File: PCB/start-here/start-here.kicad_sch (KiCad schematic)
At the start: 23 parts, among them J1 RJ45_Hanrun_HR911105A_Horizon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, U1 STM32F439ZITx, U2 LAN8742A, U3 AP7361C-10E, Y1 Crystal_GND24

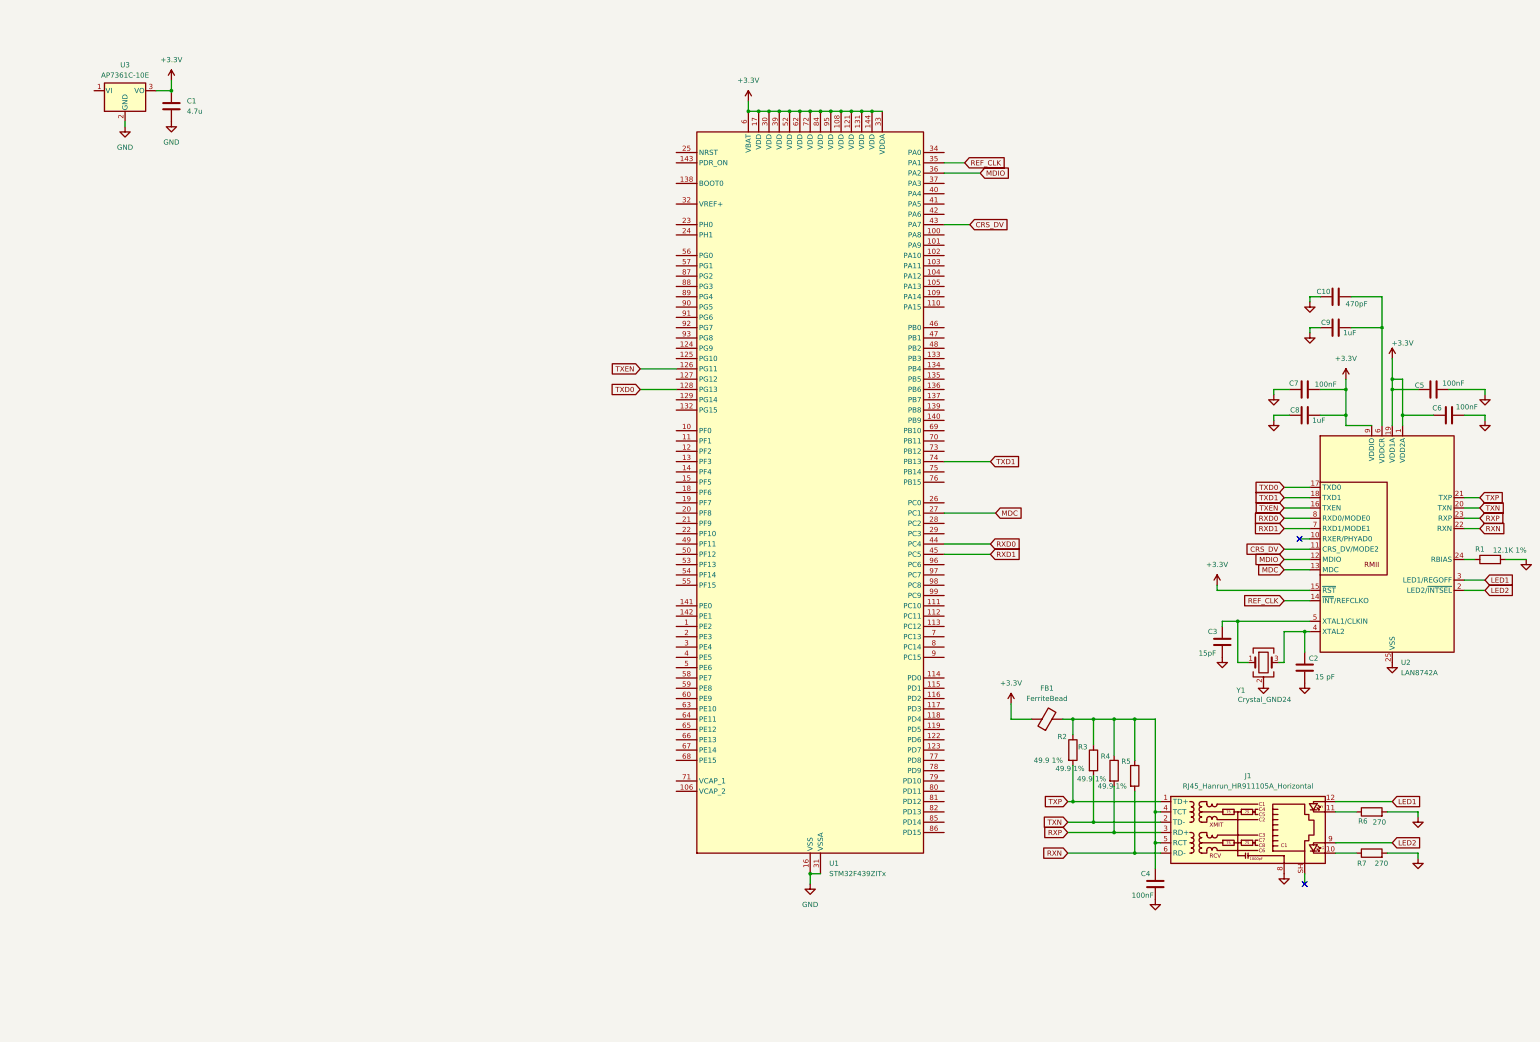
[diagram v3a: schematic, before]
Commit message: schematic done, but not verified
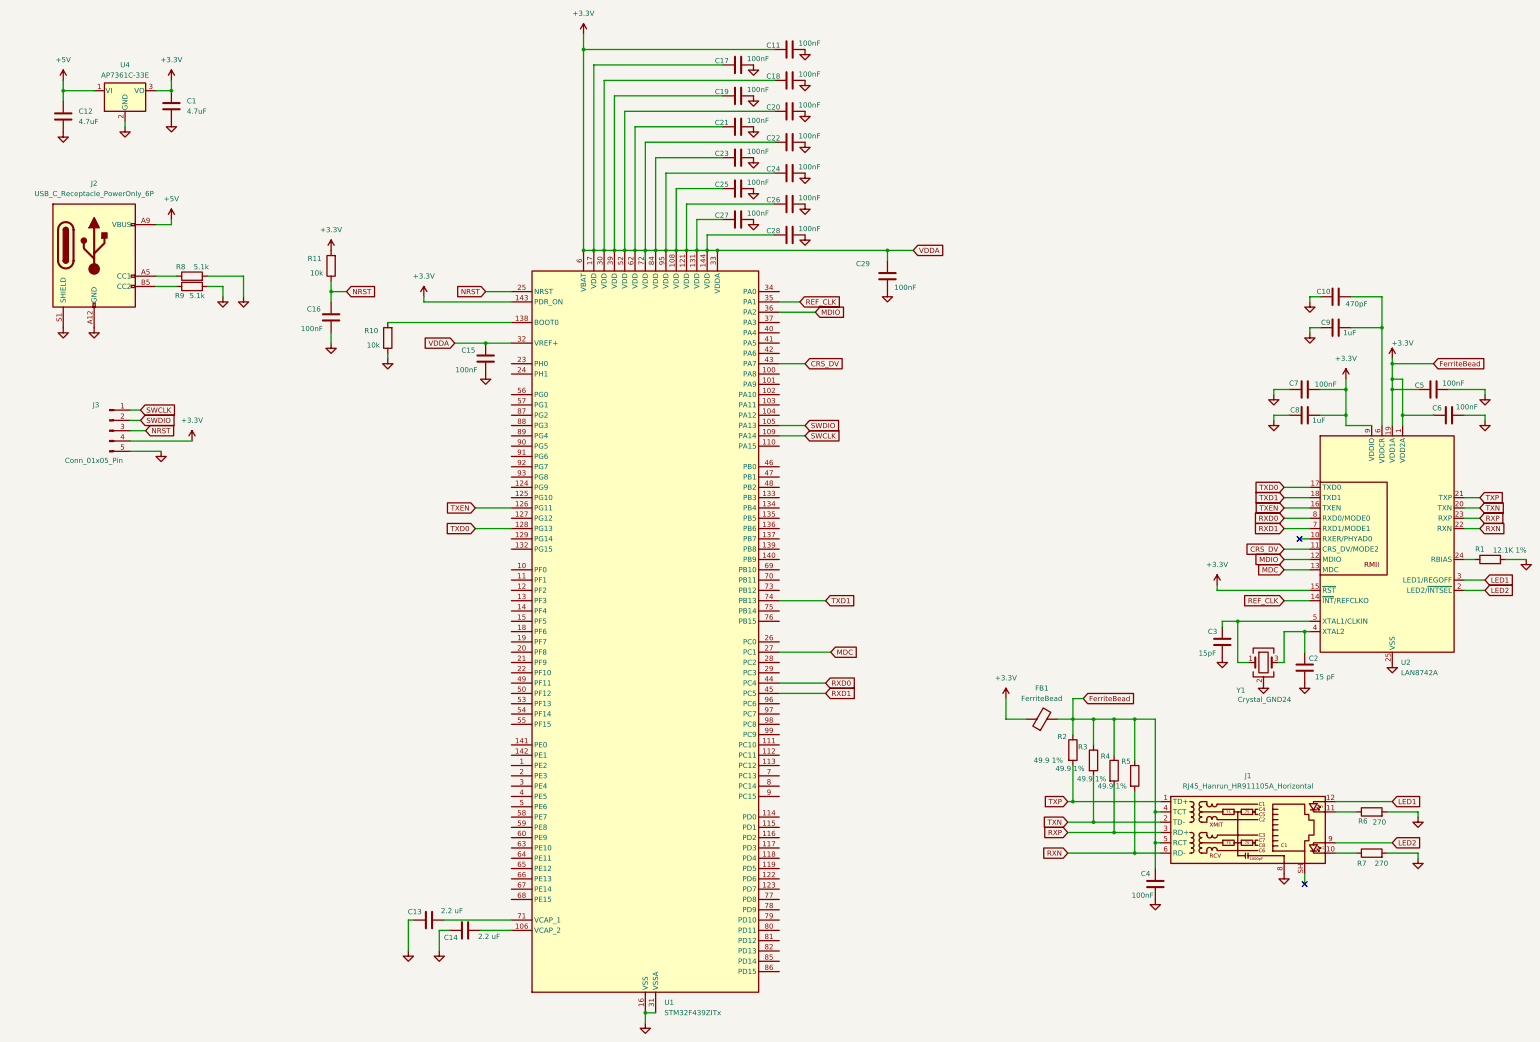
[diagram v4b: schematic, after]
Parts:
- removed U3: AP7361C-10E, Package_TO_SOT_SMD:SOT-223-3_TabPin2, symbol Regulator_Linear:AP7361C-10E
- added C11, C15, C16, C17, C18, C19, C20, C21, C22, C23, C24, C25, C26, C27, C28, C29: 100nF, symbol Device:C
- added C12: 4.7uF, Capacitor_SMD:C_1206_3216Metric, symbol Device:C
- added C13, C14: 2.2 uF, symbol Device:C
- added J2: USB_C_Receptacle_PowerOnly_6P, symbol Connector:USB_C_Receptacle_PowerOnly_6P
- added J3: Conn_01x05_Pin, symbol Connector:Conn_01x05_Pin
- added R10, R11: 10k, symbol Device:R
- added R8, R9: 5.1k, symbol Device:R
- added U4: AP7361C-33E, Package_TO_SOT_SMD:SOT-223-3_TabPin2, symbol Regulator_Linear:AP7361C-33E
- C1: value 4.7u -> 4.7uF
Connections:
- net +3.3V: now also C4.1, FB1.2, J1.4 (TCT), J1.5 (RCT), R2.1, R3.1, R4.1, R5.1, U1.143 (PDR_ON), U1.32 (VREF+), C11.1, C15.2, C17.1, C18.1, C19.1, C20.1, C21.1, C22.1, C23.1, C24.1, C25.1, C26.1, C27.1, C28.1, C29.2, J3.4 (Pin_4), R11.2, U4.3 (VO)
- net GND: now also C11.2, C12.2, C13.1, C14.1, C15.1, C16.1, C17.2, C18.2, C19.2, C20.2, C21.2, C22.2, C23.2, C24.2, C25.2, C26.2, C27.2, C28.2, C29.1, J2.A12 (GND), J2.B12 (GND), J2.S1 (SHIELD), J3.5 (Pin_5), R10.1, R8.2, R9.2, U4.2 (GND)
- net SWDIO: now reaches U1.105 (PA13)
- net SWDIO: now also J3.2 (Pin_2)
- net at U1.106 (VCAP_2): now also C14.2
- net SWCLK: now reaches U1.109 (PA14)
- net SWCLK: now also J3.1 (Pin_1)
- net at U1.138 (BOOT0): now also R10.2
- net NRST: now reaches U1.25 (NRST)
- net NRST: now also C16.2, J3.3 (Pin_3), R11.1
- net at U1.71 (VCAP_1): now also C13.2
- new net: J2.B5 (CC2), R9.1
- new net: J2.A5 (CC1), R8.1
- new net +5V: C12.1, J2.A9 (VBUS), J2.B9 (VBUS), U4.1 (VI)
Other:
- moved on the sheet: FB1, U1

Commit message: schematic done, no footprints
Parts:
- removed J3: Conn_01x05_Pin, symbol Connector:Conn_01x05_Pin
- added C3, C4: 100nF, symbol Device:C
- added J2: Conn_ARM_SWD_TagConnect_TC2030, Connector:Tag-Connect_TC2030-IDC-FP_2x03_P1.27mm_Vertical, symbol Connector:Conn_ARM_SWD_TagConnect_TC2030
- J1: renamed from J2; footprint (none) -> Connector_USB:USB_C_Receptacle_GCT_USB4125-xx-x-0190_6P_TopMnt_Horizontal
- renumbered C12 to C1, C19 to C10, C21 to C11, C23 to C12, C25 to C13, C27 to C14, C11 to C15, C18 to C16, C20 to C17, C22 to C18, C24 to C19, C1 to C2, C26 to C20, C28 to C21, C29 to C22, C4 to C23, C3 to C24, C7 to C25, C8 to C26, C2 to C27, C10 to C28, C9 to C29, C5 to C30, C6 to C31, C16 to C5, C13 to C6, C14 to C7, C15 to C8, C17 to C9, J1 to J3, R8 to R1, R7 to R10, R1 to R11, R9 to R2, R11 to R3, R10 to R4, R2 to R5, R3 to R6, R4 to R7, R5 to R8, R6 to R9, U4 to U1, U1 to U2, U2 to U3
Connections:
- net +3.3V: now also C3.2, C4.2, J2.1 (VCC)
- net GND: now also C3.1, C4.1, J2.5 (GND)
- net NRST: now also J2.3 (~{RESET})
- net SWCLK: now also J2.4 (SWCLK)
- net SWDIO: now also J2.2 (SWDIO)
- net SWO: now reaches U2.133 (PB3)
- net SWO: now also J2.6 (SWO)
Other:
- moved on the sheet: C5, R3, R4

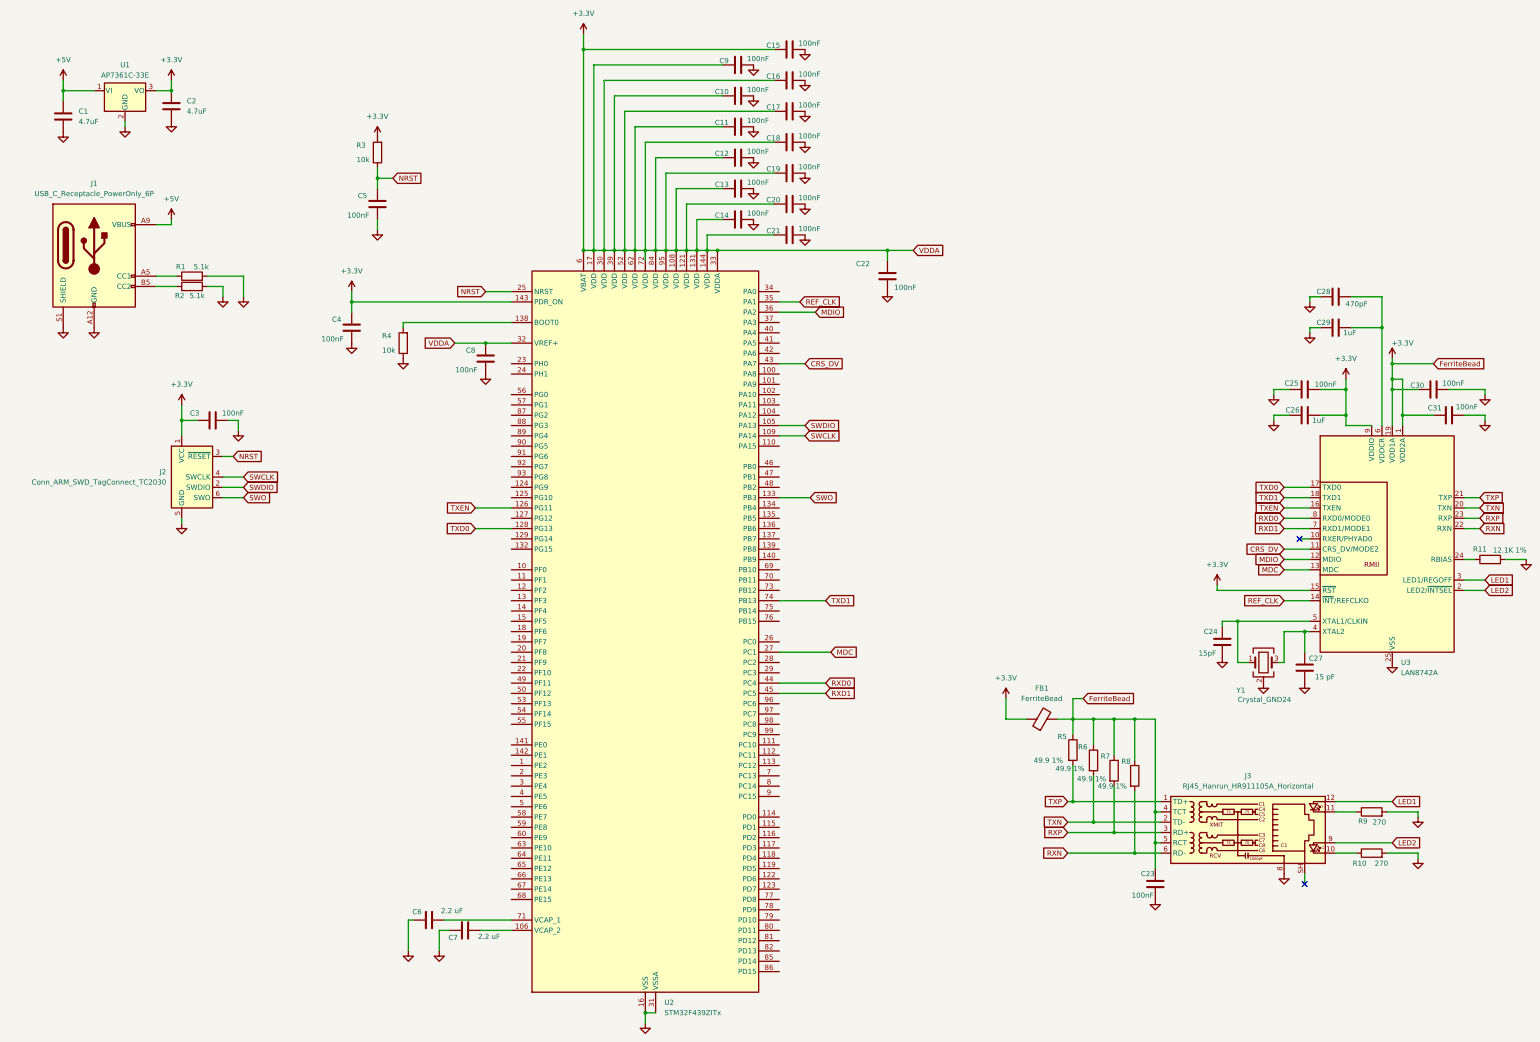
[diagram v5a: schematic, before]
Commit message: add footprints to components and fix ECR
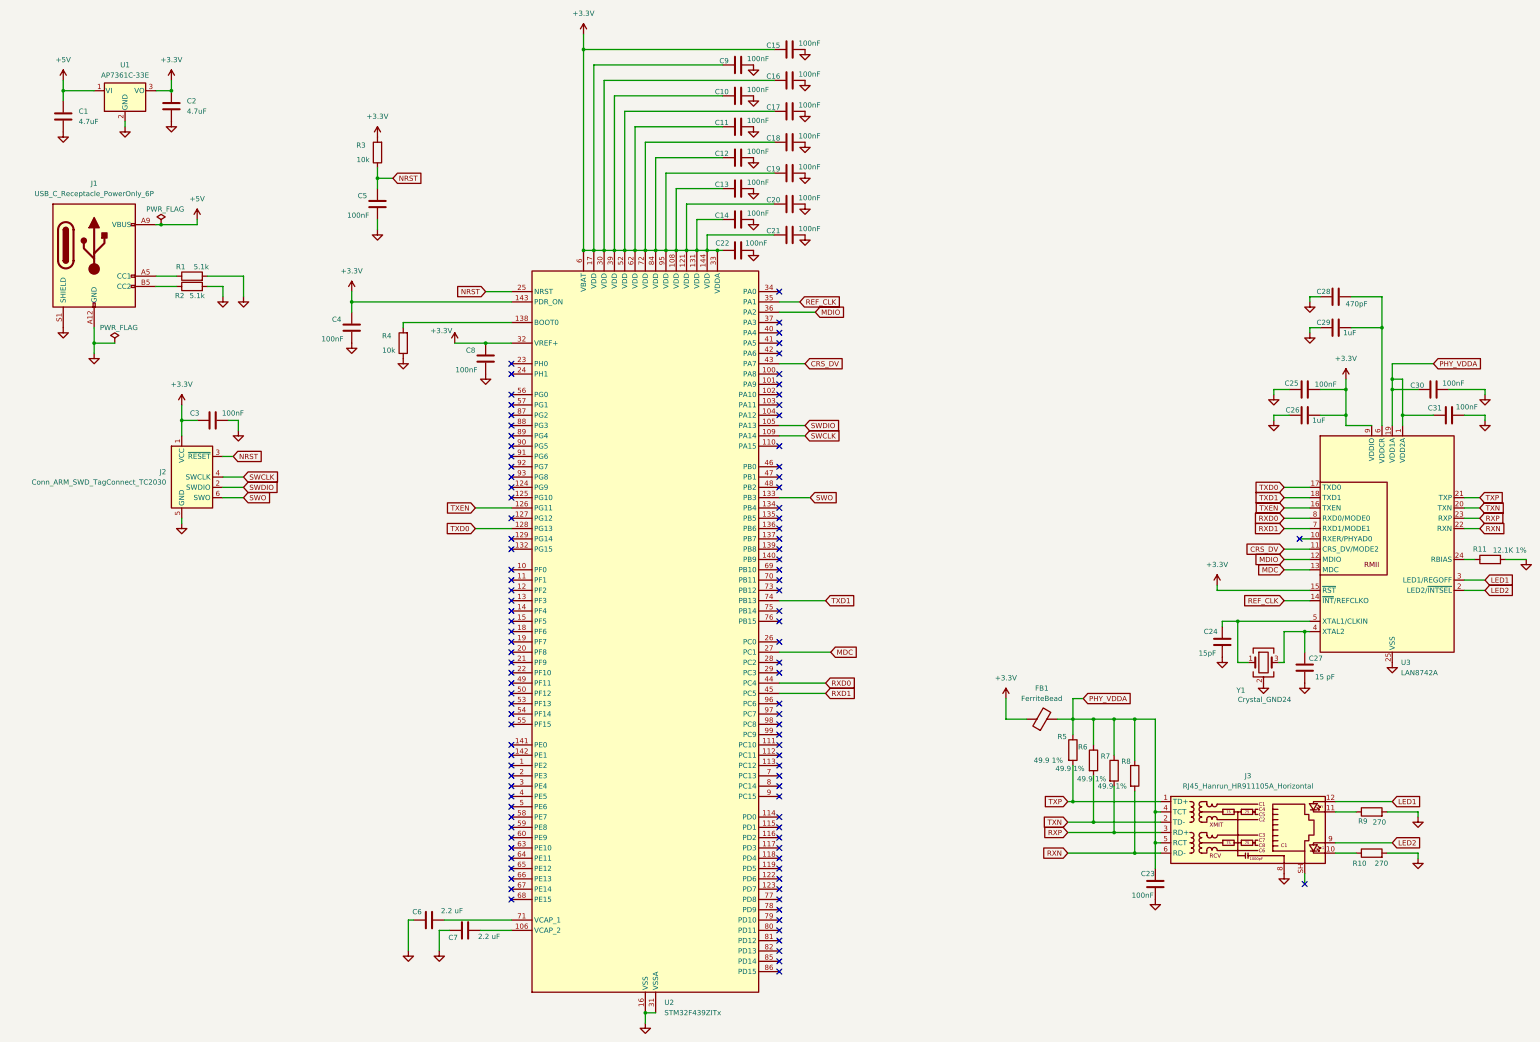
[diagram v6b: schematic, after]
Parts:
- C1, C2: footprint Capacitor_SMD:C_1206_3216Metric -> Capacitor_SMD:C_0603_1608Metric
- C10, C11, C12, C13, C14, C15, C16, C17, C18, C19, C20, C21, C22, C23, C24, C25, C26, C27, C28, C29, C3, C30, C31, C4, C5, C6, C7, C8, C9: footprint (none) -> Capacitor_SMD:C_0603_1608Metric
- FB1, R1, R10, R11, R2, R3, R4, R5, R6, R7, R8, R9: footprint (none) -> Resistor_SMD:R_0603_1608Metric
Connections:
- net +3.3V: no longer C23.1, C30.1, C31.1, FB1.2, J3.4 (TCT), J3.5 (RCT), R5.1, R6.1, R7.1, R8.1, U3.1 (VDD2A), U3.19 (VDD1A)
- new net PHY_VDDA: C23.1, C30.1, C31.1, FB1.2, J3.4 (TCT), J3.5 (RCT), R5.1, R6.1, R7.1, R8.1, U3.1 (VDD2A), U3.19 (VDD1A)
- no-connect marks 2 -> 104
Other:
- moved on the sheet: C22
